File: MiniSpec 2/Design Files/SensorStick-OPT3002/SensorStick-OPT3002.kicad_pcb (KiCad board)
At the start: 2 copper layers, 14 x 25 mm, 6 parts, among them IC1 OPT3002DNPT, J1 TSM-104-02-S-DV-P-TR

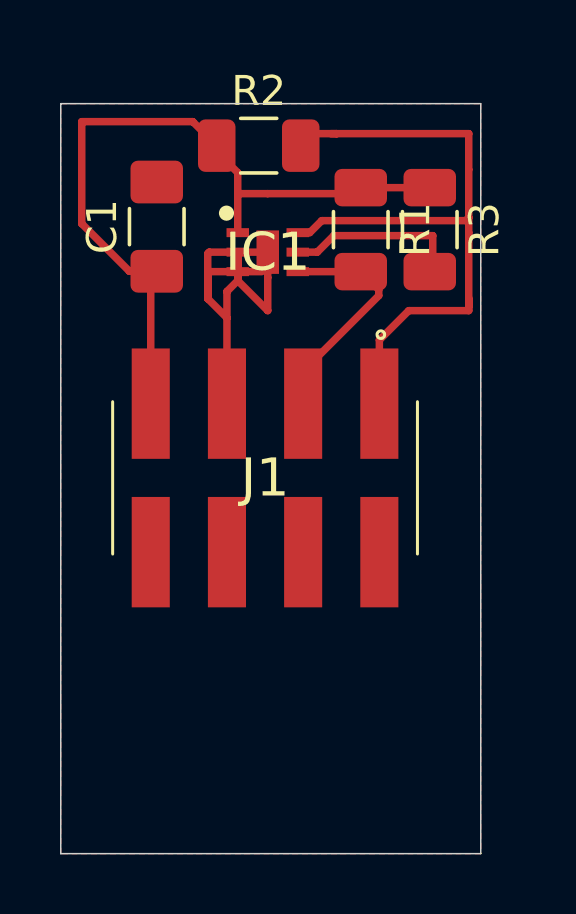
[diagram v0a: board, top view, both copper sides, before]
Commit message: big updates for 2 layer design with vias
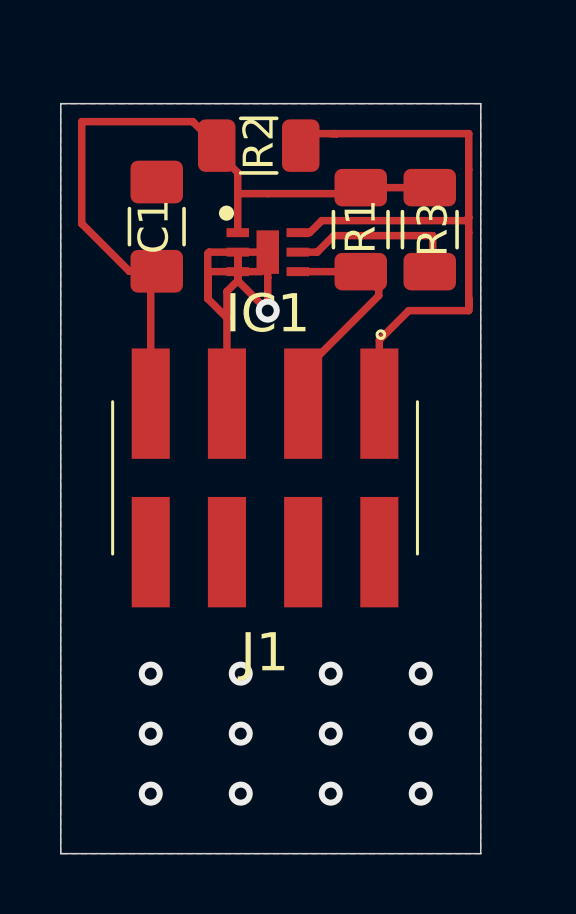
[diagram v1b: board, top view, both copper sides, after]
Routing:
- net GND: vias 0 -> 13
- added copper zone on B.Cu, net GND
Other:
- board text added: "Sensor OPT"
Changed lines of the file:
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@@
-(kicad_pcb (version 20171130) (host pcbnew "(5.1.6)-1")
+(kicad_pcb (version 20171130) (host pcbnew "(5.1.9)-1")
   (general
     (thickness 1.6)
-    (drawings 8)
-    (tracks 73)
+    (drawings 9)
+    (tracks 87)
     (zones 0)
     (modules 6)
@@
   (layers
     (0 F.Cu signal)
-    (31 B.Cu signal hide)
-    (32 B.Adhes user hide)
-    (33 F.Adhes user hide)
-    (34 B.Paste user hide)
-    (35 F.Paste user hide)
-    (36 B.SilkS user hide)
-    (37 F.SilkS user hide)
-    (38 B.Mask user hide)
-    (39 F.Mask user hide)
+    (31 B.Cu signal)
+    (32 B.Adhes user)
+    (33 F.Adhes user)
+    (34 B.Paste user)
+    (35 F.Paste user)
+    (36 B.SilkS user)
+    (37 F.SilkS user)
+    (38 B.Mask user)
+    (39 F.Mask user)
     (40 Dwgs.User user)
     (41 Cmts.User user hide)
@@
     (visible_elements 7FFFFFFF)
     (pcbplotparams
-      (layerselection 0x00000_7fffffff)
+      (layerselection 0x3ffff_ffffffff)
       (usegerberextensions false)
       (usegerberattributes true)
@@
       (hpglpenspeed 20)
       (hpglpendiameter 15.000000)
-      (psnegative true)
+      (psnegative false)
       (psa4output false)
       (plotreference true)
@@
       (padsonsilk false)
       (subtractmaskfromsilk false)
-      (outputformat 4)
+      (outputformat 1)
       (mirror false)
       (drillshape 0)
       (scaleselection 1)
-      (outputdirectory ""))
+      (outputdirectory "../../../../../../Desktop/Temp MiniSpec/"))
   )
   (net 0 "")
@@
     (tags resistor)
     (attr smd)
-    (fp_text reference R1 (at 0 -1.82 90) (layer F.SilkS)
+    (fp_text reference R1 (at -0.1 0 90) (layer F.SilkS)
       (effects (font (size 1 1) (thickness 0.15)))
     )
@@
     (tags Connector)
     (attr smd)
-    (fp_text reference J1 (at 0 0) (layer F.SilkS)
+    (fp_text reference J1 (at -0.01 5.825) (layer F.SilkS)
       (effects (font (size 1.27 1.27) (thickness 0.254)))
     )
-    (fp_text value TSM-104-02-S-DV-P-TR (at 0 0) (layer F.SilkS) hide
+    (fp_text value TSM-104-02-S-DV-P-TR (at -8.11 0.025 90) (layer F.SilkS) hide
       (effects (font (size 1.27 1.27) (thickness 0.254)))
     )
@@
     (tags "Integrated Circuit")
     (attr smd)
-    (fp_text reference IC1 (at 0 0) (layer F.SilkS)
+    (fp_text reference IC1 (at 0 2.05) (layer F.SilkS)
       (effects (font (size 1.27 1.27) (thickness 0.254)))
     )
@@
     (tags resistor)
     (attr smd)
-    (fp_text reference R3 (at 0 -1.82 90) (layer F.SilkS)
+    (fp_text reference R3 (at 0 -0.1 90) (layer F.SilkS)
       (effects (font (size 1 1) (thickness 0.15)))
     )
@@
     (tags resistor)
     (attr smd)
-    (fp_text reference R2 (at 0 -1.82) (layer F.SilkS)
+    (fp_text reference R2 (at 0 -0.1 90) (layer F.SilkS)
       (effects (font (size 1 1) (thickness 0.15)))
     )
@@
     (tags "capacitor handsolder")
     (attr smd)
-    (fp_text reference C1 (at 0 -1.82 90) (layer F.SilkS)
+    (fp_text reference C1 (at 0 -0.1 90) (layer F.SilkS)
       (effects (font (size 1 1) (thickness 0.15)))
     )
@@
       (effects (font (size 0.8 0.8) (thickness 0.12)))
     )
-    (pad 2 smd roundrect (at 1.4875 0 90) (size 1.425 1.75) (layers F.Cu F.Paste F.Mask) (roundrect_rratio 0.175439)
-      (net 1 GND))
-    (pad 1 smd roundrect (at -1.4875 0 90) (size 1.425 1.75) (layers F.Cu F.Paste F.Mask) (roundrect_rratio 0.175439)
+    (pad 2 smd roundrect (at 1.4875 0 90) (size 1.425 1.75) (layers F.Cu F.Paste F.Mask) (roundrect_rratio 0.1754385964912281)
+      (net 1 GND))
+    (pad 1 smd roundrect (at -1.4875 0 90) (size 1.425 1.75) (layers F.Cu F.Paste F.Mask) (roundrect_rratio 0.1754385964912281)
       (net 2 +3V3))
     (model ${KISYS3DMOD}/Capacitor_SMD.3dshapes/C_1206_3216Metric.wrl
@@
       (rotate (xyz 0 0 0))
     )
+  )
+  (gr_text "Sensor OPT" (at 138 73) (layer B.Mask)
+    (effects (font (size 1 1) (thickness 0.15)) (justify mirror))
   )
   (gr_line (start 130 155) (end 130 60) (layer Eco2.User) (width 0.15))
@@
   (segment (start 137.9 66.95) (end 137.95 66.95) (width 0.25) (layer F.Cu) (net 1))
   (segment (start 136.9 67.9) (end 136.9 67.6) (width 0.25) (layer F.Cu) (net 1))
-  (segment (start 137.9 68.9) (end 136.9 67.9) (width 0.25) (layer F.Cu) (net 1))
+  (segment (start 137.9 68.9) (end 137.9 68.9) (width 0.25) (layer F.Cu) (net 1))
   (segment (start 136.9 66.95) (end 136.9 67.9) (width 0.25) (layer F.Cu) (net 1))
   (segment (start 136.9 67.9) (end 136.54 68.26) (width 0.25) (layer F.Cu) (net 1))
@@
   (segment (start 137.9 66.95) (end 137.9 67.8) (width 0.25) (layer F.Cu) (net 1))
   (segment (start 137.9 67.8) (end 137.9 68.9) (width 0.25) (layer F.Cu) (net 1))
+  (via (at 134 81) (size 0.8) (drill 0.4) (layers F.Cu B.Cu) (net 1))
+  (via (at 137 81) (size 0.8) (drill 0.4) (layers F.Cu B.Cu) (net 1))
+  (via (at 140 81) (size 0.8) (drill 0.4) (layers F.Cu B.Cu) (net 1))
+  (via (at 143 81) (size 0.8) (drill 0.4) (layers F.Cu B.Cu) (net 1))
+  (via (at 134 83) (size 0.8) (drill 0.4) (layers F.Cu B.Cu) (net 1))
+  (via (at 137 83) (size 0.8) (drill 0.4) (layers F.Cu B.Cu) (net 1))
+  (via (at 140 83) (size 0.8) (drill 0.4) (layers F.Cu B.Cu) (net 1))
+  (via (at 143 83) (size 0.8) (drill 0.4) (layers F.Cu B.Cu) (net 1))
+  (via (at 134 85) (size 0.8) (drill 0.4) (layers F.Cu B.Cu) (net 1))
+  (via (at 137 85) (size 0.8) (drill 0.4) (layers F.Cu B.Cu) (net 1))
+  (via (at 140 85) (size 0.8) (drill 0.4) (layers F.Cu B.Cu) (net 1))
+  (via (at 143 85) (size 0.8) (drill 0.4) (layers F.Cu B.Cu) (net 1))
+  (segment (start 137.9 68.9) (end 136.9 67.9) (width 0.25) (layer F.Cu) (net 1))
+  (via (at 137.9 68.9) (size 0.8) (drill 0.4) (layers F.Cu B.Cu) (net 1))
   (segment (start 134 67.9875) (end 134.4 67.5875) (width 0.25) (layer F.Cu) (net 2))
   (segment (start 134 72) (end 134 67.9875) (width 0.25) (layer F.Cu) (net 2))
@@
     (connect_pads (clearance 0.508))
     (min_thickness 0.254)
+    (fill yes (arc_segments 32) (thermal_gap 0.508) (thermal_bridge_width 0.508))
+    (polygon
+      (pts
+        (xy 145 87) (xy 131 87) (xy 131 62) (xy 145 62)
+      )
+    )
+  )
+  (zone (net 1) (net_name GND) (layer B.Cu) (hatch edge 0.508)
+    (connect_pads (clearance 0.508))
+    (min_thickness 0.254)
